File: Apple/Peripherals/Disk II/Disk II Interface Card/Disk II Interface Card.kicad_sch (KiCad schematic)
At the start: 28 parts, among them J1 50 Pin Edge, J2 DRIVE 2, J3 DRIVE 1, Q1 2N3906, Q2 MPSU51, Q3 MPSU51

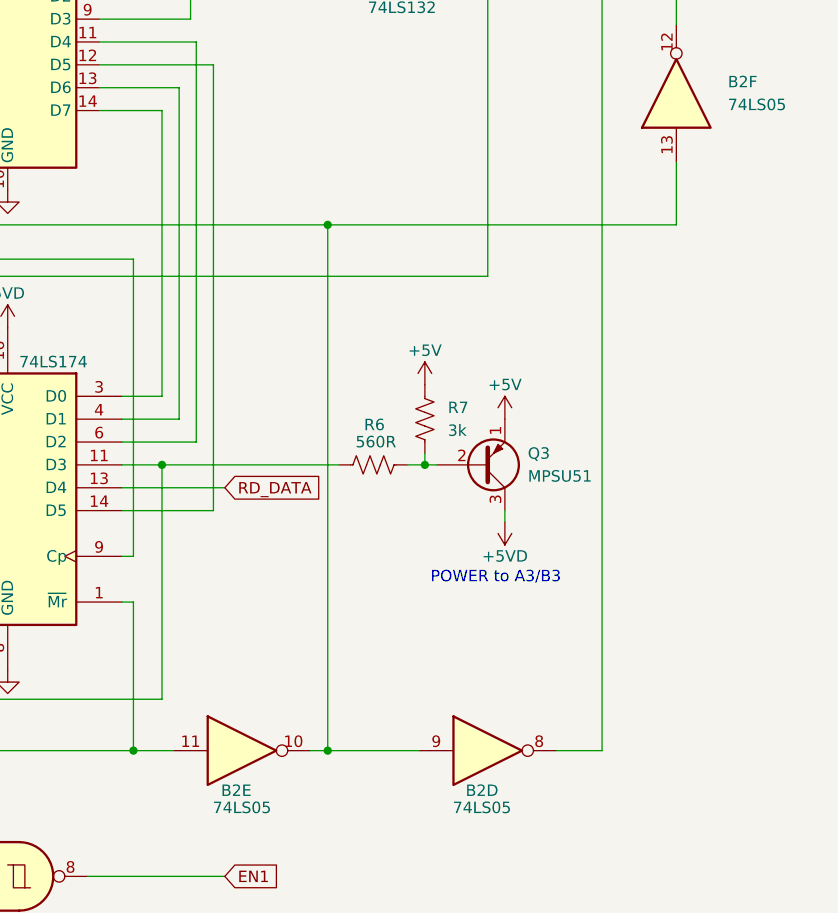
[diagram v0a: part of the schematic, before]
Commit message: FIX: B2E, pin 10 missing junction. B2F connected to wrong node. FIX: B2F, 13 was not connected to correct node.
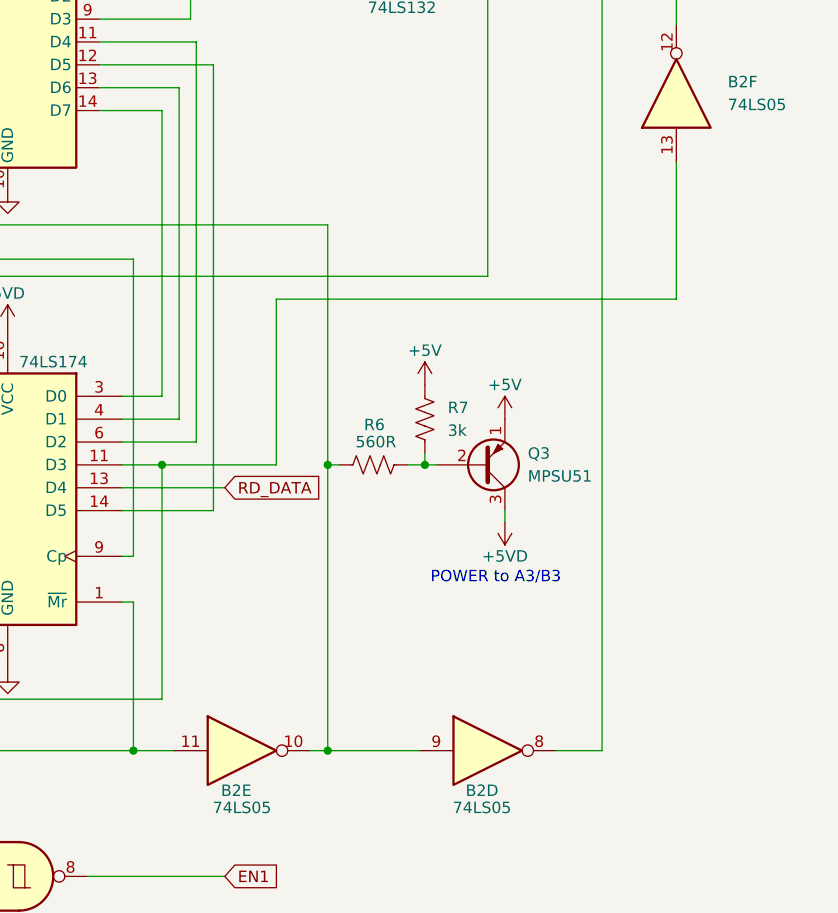
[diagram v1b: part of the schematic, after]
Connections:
- net at B2.10, B2.9, B3.16 (E2): now also R6.1; no longer B2.13
- net at A3.11 (D3), A3.12 (Q4): now also B2.13; no longer R6.1
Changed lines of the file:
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@@
   (junction (at 192.405 45.72) (diameter 0) (color 0 0 0 0)
   )
+  (junction (at 109.22 160.02) (diameter 0) (color 0 0 0 0)
+  )
+  (junction (at 186.69 138.43) (diameter 0) (color 0 0 0 0)
+  )
+  (junction (at 335.28 102.235) (diameter 0) (color 0 0 0 0)
+  )
   (junction (at 233.045 95.25) (diameter 0) (color 0 0 0 0)
   )
-  (junction (at 109.22 160.02) (diameter 0) (color 0 0 0 0)
-  )
-  (junction (at 186.69 138.43) (diameter 0) (color 0 0 0 0)
-  )
-  (junction (at 335.28 102.235) (diameter 0) (color 0 0 0 0)
-  )
   (junction (at 129.54 45.72) (diameter 0) (color 0 0 0 0)
   )
@@
   (junction (at 354.33 94.615) (diameter 0) (color 0 0 0 0)
   )
-  (junction (at 251.46 68.58) (diameter 0) (color 0 0 0 0)
-  )
   (junction (at 207.01 152.4) (diameter 0) (color 0 0 0 0)
   )
@@
   )
   (junction (at 74.295 160.02) (diameter 0) (color 0 0 0 0)
+  )
+  (junction (at 251.46 95.25) (diameter 0) (color 0 0 0 0)
   )
   (junction (at 335.28 97.155) (diameter 0) (color 0 0 0 0)
@@
     (stroke (width 0) (type default))
   )
+  (wire (pts (xy 251.46 95.25) (xy 251.46 127))
+    (stroke (width 0) (type default))
+  )
   (wire (pts (xy 50.8 48.26) (xy 55.88 48.26))
     (stroke (width 0) (type default))
@@
     (stroke (width 0) (type default))
   )
-  (wire (pts (xy 251.46 68.58) (xy 290.195 68.58))
-    (stroke (width 0) (type default))
-  )
   (wire (pts (xy 234.315 38.1) (xy 226.06 38.1))
     (stroke (width 0) (type default))
@@
     (stroke (width 0) (type default))
   )
+  (wire (pts (xy 233.045 95.25) (xy 245.745 95.25))
+    (stroke (width 0) (type default))
+  )
   (bus (pts (xy 93.98 60.96) (xy 93.98 58.42))
     (stroke (width 0) (type default))
@@
     (stroke (width 0) (type default))
   )
+  (wire (pts (xy 245.745 76.835) (xy 290.195 76.835))
+    (stroke (width 0) (type default))
+  )
+  (wire (pts (xy 290.195 76.835) (xy 290.195 61.595))
+    (stroke (width 0) (type default))
+  )
   (bus (pts (xy 129.54 58.42) (xy 129.54 55.88))
     (stroke (width 0) (type default))
@@
     (stroke (width 0) (type default))
   )
-  (wire (pts (xy 251.46 68.58) (xy 251.46 127))
+  (wire (pts (xy 251.46 68.58) (xy 251.46 95.25))
     (stroke (width 0) (type default))
   )
@@
     (stroke (width 0) (type default))
   )
-  (wire (pts (xy 290.195 61.595) (xy 290.195 68.58))
-    (stroke (width 0) (type default))
-  )
   (bus (pts (xy 129.54 13.97) (xy 140.97 13.97))
     (stroke (width 0) (type default))
@@
     (stroke (width 0) (type default))
   )
+  (wire (pts (xy 245.745 95.25) (xy 245.745 76.835))
+    (stroke (width 0) (type default))
+  )
   (wire (pts (xy 22.86 33.02) (xy 38.1 33.02))
     (stroke (width 0) (type default))
@@
     (stroke (width 0) (type default))
   )
-  (wire (pts (xy 233.045 95.25) (xy 252.73 95.25))
-    (stroke (width 0) (type default))
-  )
   (wire (pts (xy 350.52 44.45) (xy 354.33 44.45))
     (stroke (width 0) (type default))
@@
     (stroke (width 0) (type default))
   )
+  (wire (pts (xy 251.46 95.25) (xy 252.73 95.25))
+    (stroke (width 0) (type default))
+  )

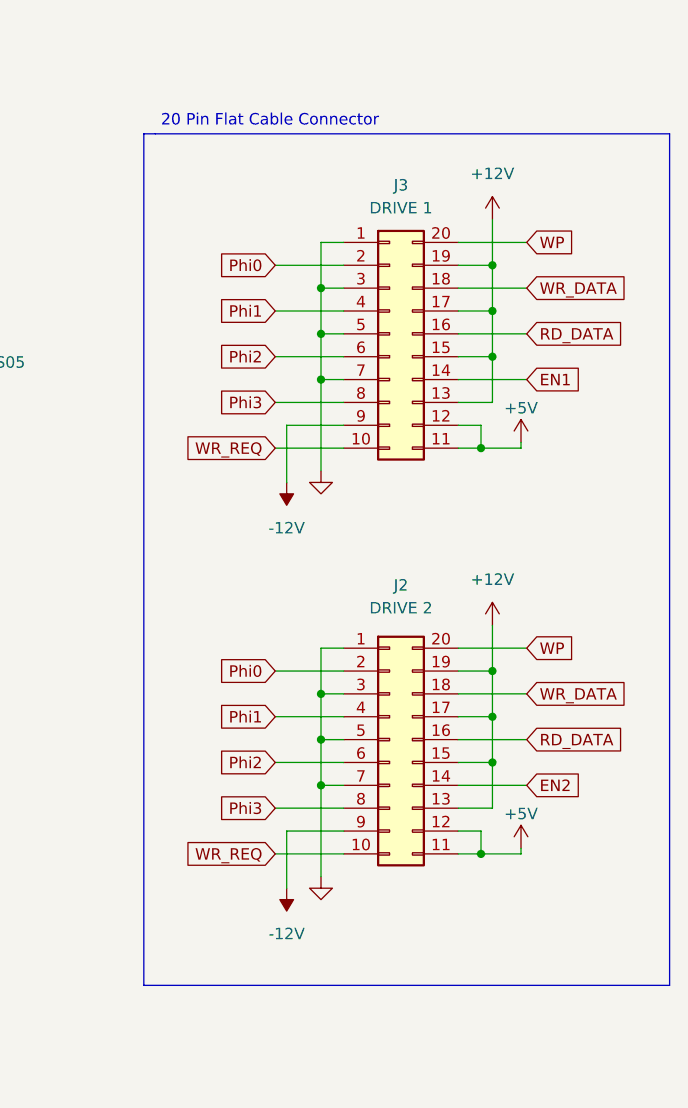
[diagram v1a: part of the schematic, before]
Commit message: redrew 20-pin to match pysical pinout (odd-even)
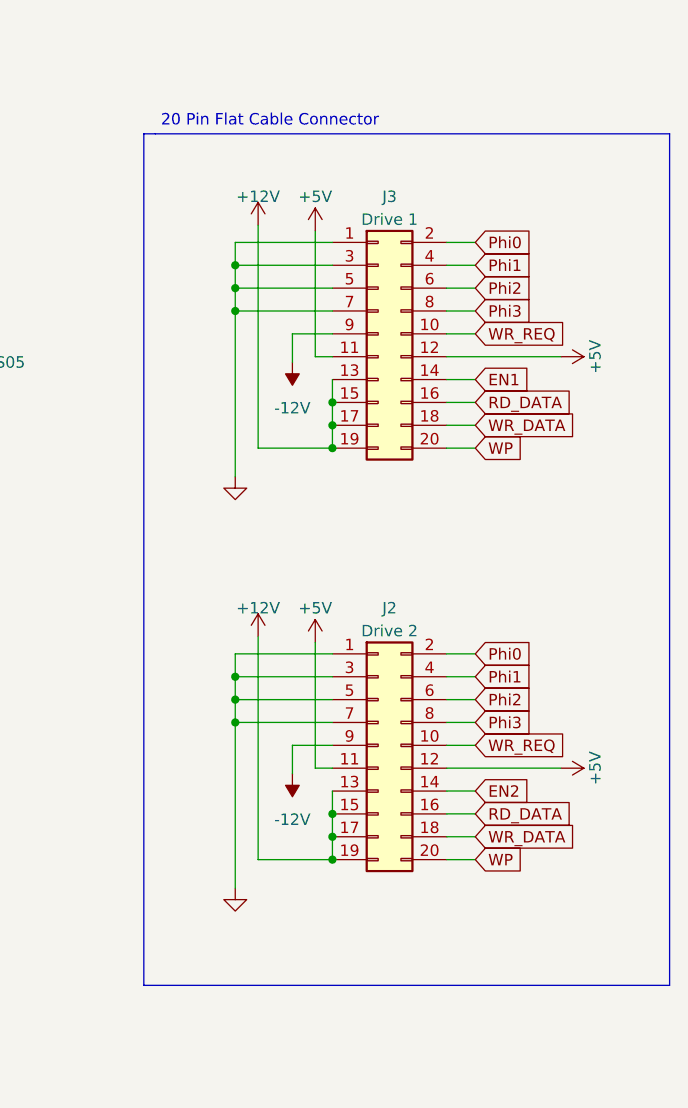
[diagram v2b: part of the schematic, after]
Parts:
- removed J2: DRIVE 2, symbol Connector_Generic:Conn_02x10_Counter_Clockwise
- removed J3: DRIVE 1, symbol Connector_Generic:Conn_02x10_Counter_Clockwise
- added J2: Drive 2, symbol Connector_Generic:Conn_02x10_Odd_Even
- added J3: Drive 1, symbol Connector_Generic:Conn_02x10_Odd_Even
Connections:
- net +12V: now also J2.13 (Pin_13), J2.15 (Pin_15), J2.17 (Pin_17), J2.19 (Pin_19), J3.13 (Pin_13), J3.15 (Pin_15), J3.17 (Pin_17), J3.19 (Pin_19)
- net +5V: now also J2.11 (Pin_11), J2.12 (Pin_12), J3.11 (Pin_11), J3.12 (Pin_12)
- net -12V: now also J2.9 (Pin_9), J3.9 (Pin_9)
- net EN1: now also J3.14 (Pin_14)
- net EN2: now also J2.14 (Pin_14)
- net GND: now also J2.1 (Pin_1), J2.3 (Pin_3), J2.5 (Pin_5), J2.7 (Pin_7), J3.1 (Pin_1), J3.3 (Pin_3), J3.5 (Pin_5), J3.7 (Pin_7)
- net Phi0: now also J2.2 (Pin_2), J3.2 (Pin_2)
- net Phi1: now also J2.4 (Pin_4), J3.4 (Pin_4)
- net Phi2: now also J2.6 (Pin_6), J3.6 (Pin_6)
- net Phi3: now also J2.8 (Pin_8), J3.8 (Pin_8)
- net RD_DATA: now also J2.16 (Pin_16), J3.16 (Pin_16)
- net WP: now also J2.20 (Pin_20), J3.20 (Pin_20)
- net WR_DATA: now also J2.18 (Pin_18), J3.18 (Pin_18)
- net WR_REQ: now also J2.10 (Pin_10), J3.10 (Pin_10)

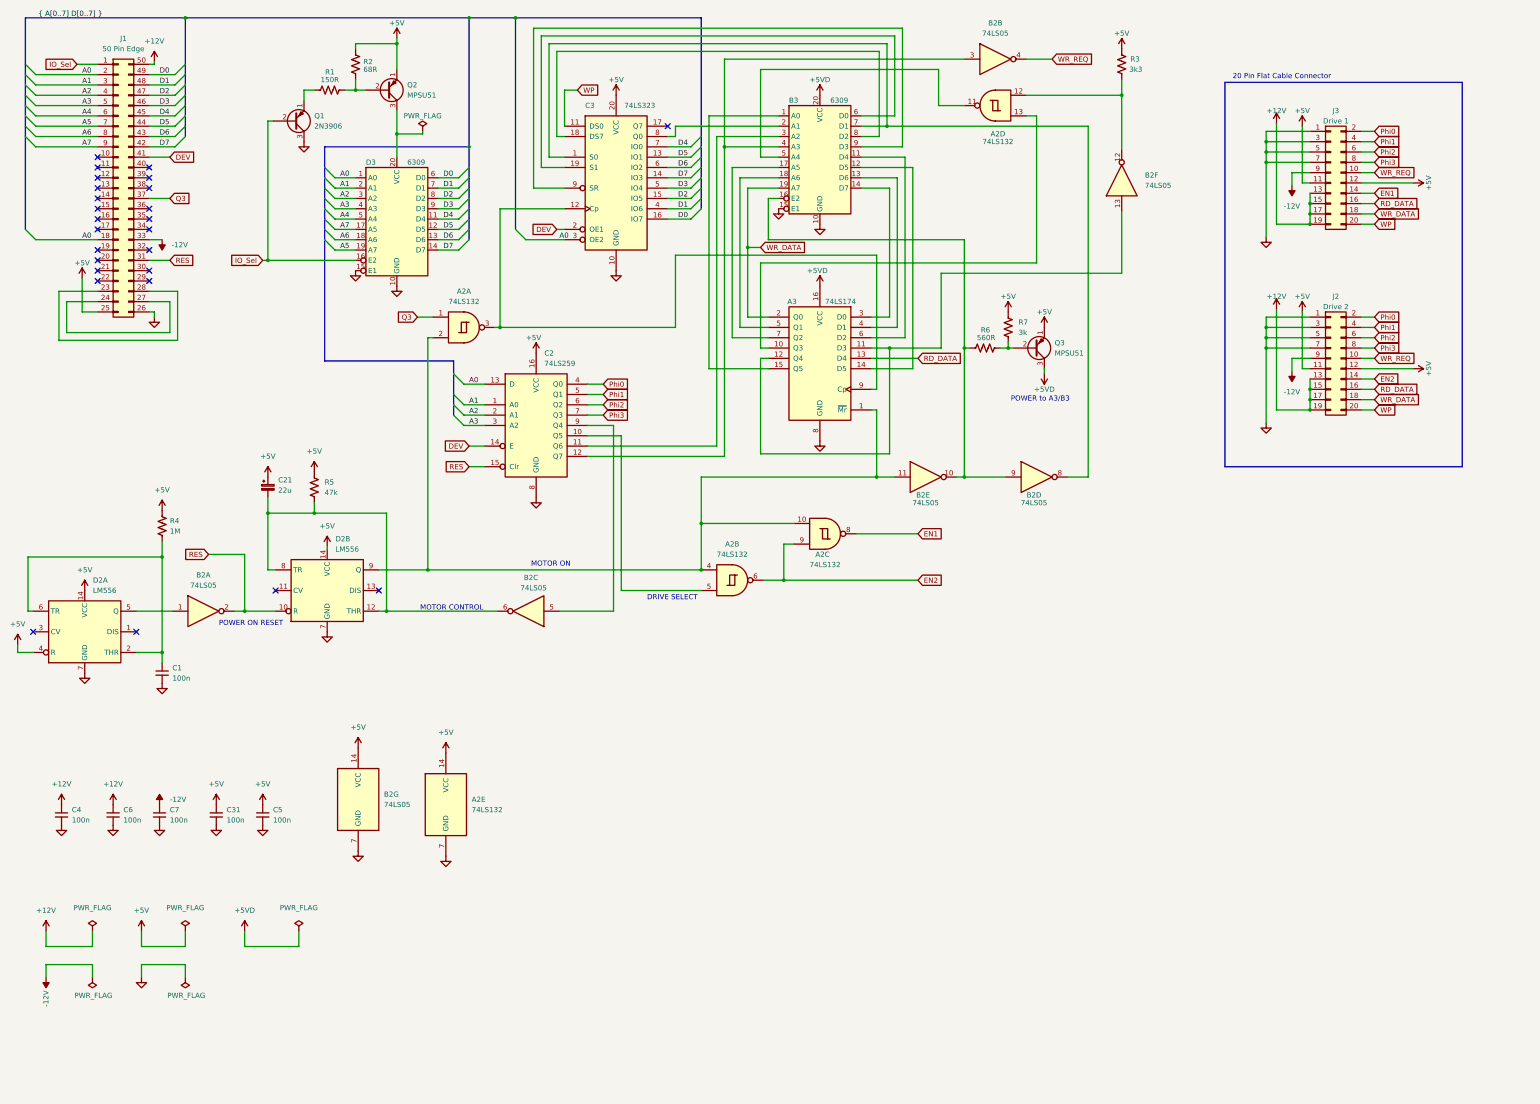
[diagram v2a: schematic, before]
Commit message: Moved PWR_FLAGS to proper source locations
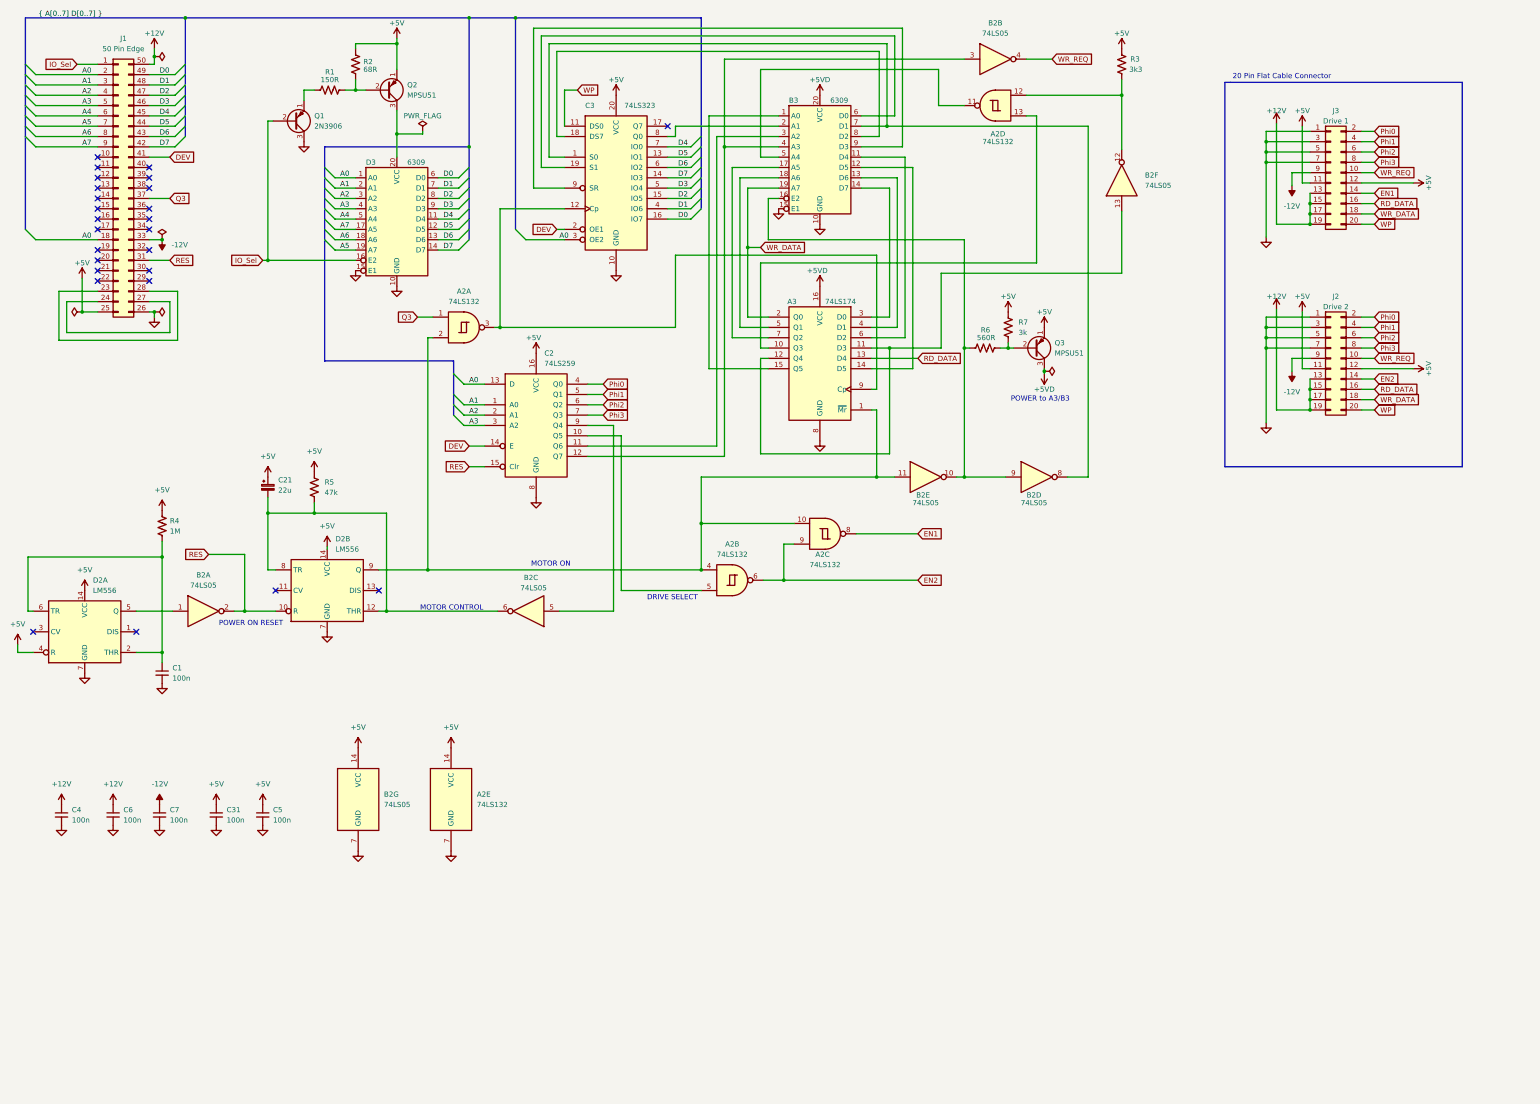
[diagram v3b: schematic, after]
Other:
- moved on the sheet: A2E

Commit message: rev2: Added PDF and updated readme.
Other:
- moved on the sheet: A2A, A2B, A2C, A2D, A2E, A3, B2A, B2B, B2C, B2D, B2E, B2F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
